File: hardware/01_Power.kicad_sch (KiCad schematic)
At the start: 59 parts, among them J1 12V IN, J5 USB-C, Q1 BUK7K17-60E, Q2 2N7002K, U1 LM74720QDRRRQ1, U2 USBLC6-2SC6, U3 TUSB321AIRWBR, U4 TPS259470LRPWR, U5 LMR33630CDDAR

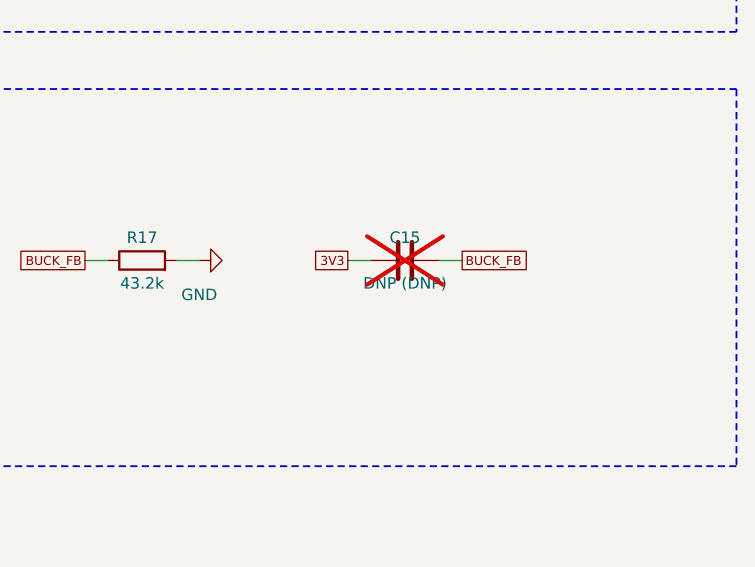
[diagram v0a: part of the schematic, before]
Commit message: Place Rev A board: 4-layer stackup, zones, two-sided placement
Generated by scripts/rebuild/gen_pcb.py from the same circuit definition.
Pre-route DRC: 0 errors, schematic parity: 0 issues.

Co-Authored-By: Claude Opus 5.5 <noreply@anthropic.com>
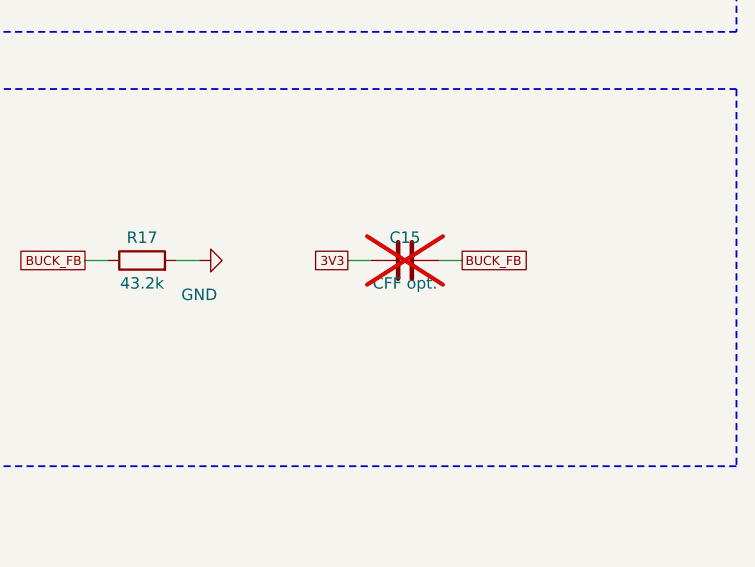
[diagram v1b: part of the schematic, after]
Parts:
- C15: value DNP (DNP) -> CFF opt.; Notes optional CFF -> optional feed-forward capacitor
- TP1, TP2, TP3, TP4, TP8: footprint TestPoint:TestPoint_Pad_D1.5mm -> TestPoint:TestPoint_Pad_D1.0mm
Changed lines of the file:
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@@
 			)
 		)
-		(property "Footprint" "TestPoint:TestPoint_Pad_D1.5mm"
+		(property "Footprint" "TestPoint:TestPoint_Pad_D1.0mm"
 			(at 369.57 63.5 0)
 			(effects
@@
 			)
 		)
-		(property "Footprint" "TestPoint:TestPoint_Pad_D1.5mm"
+		(property "Footprint" "TestPoint:TestPoint_Pad_D1.0mm"
 			(at 22.86 74.93 0)
 			(effects
@@
 			)
 		)
-		(property "Footprint" "TestPoint:TestPoint_Pad_D1.5mm"
+		(property "Footprint" "TestPoint:TestPoint_Pad_D1.0mm"
 			(at 50.8 74.93 0)
 			(effects
@@
 			)
 		)
-		(property "Footprint" "TestPoint:TestPoint_Pad_D1.5mm"
+		(property "Footprint" "TestPoint:TestPoint_Pad_D1.0mm"
 			(at 74.93 74.93 0)
 			(effects
@@
 			)
 		)
-		(property "Value" "DNP (DNP)"
+		(property "Value" "CFF opt."
 			(at 368.3 232.41 270)
 			(effects
@@
 			)
 		)
-		(property "Notes" "optional CFF"
+		(property "Notes" "optional feed-forward capacitor"
 			(at 368.3 229.87 0)
 			(effects
@@
 			)
 		)
-		(property "Footprint" "TestPoint:TestPoint_Pad_D1.5mm"
+		(property "Footprint" "TestPoint:TestPoint_Pad_D1.0mm"
 			(at 115.57 246.38 0)
 			(effects
